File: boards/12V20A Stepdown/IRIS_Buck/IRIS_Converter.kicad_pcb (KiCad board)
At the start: 4 copper layers, 64 x 48 mm, 31 parts, among them J1 TB005-762-02BE, J2 TB005-762-02BE, Q1 CSD17571Q2, Q2 CSD16340Q3, U1 LM25145RGYR

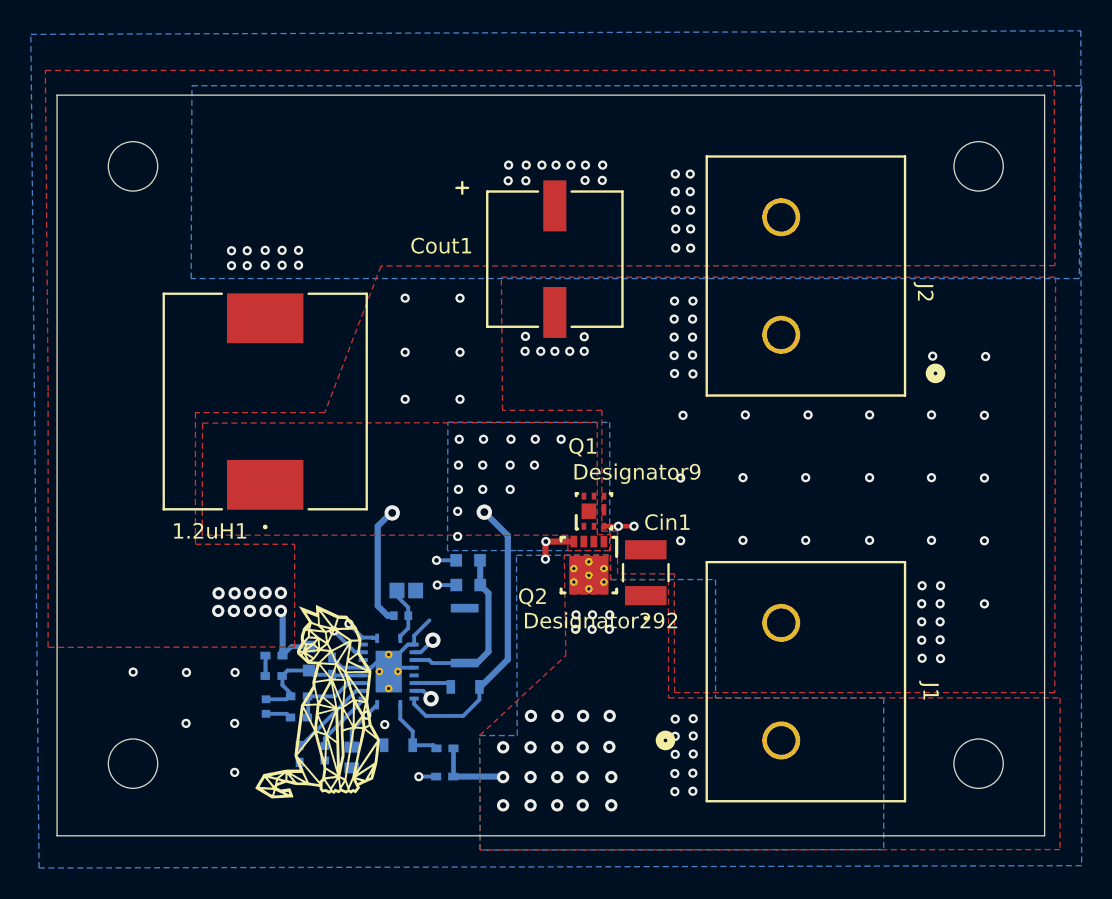
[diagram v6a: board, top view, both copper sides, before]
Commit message: removed backfill on 20a
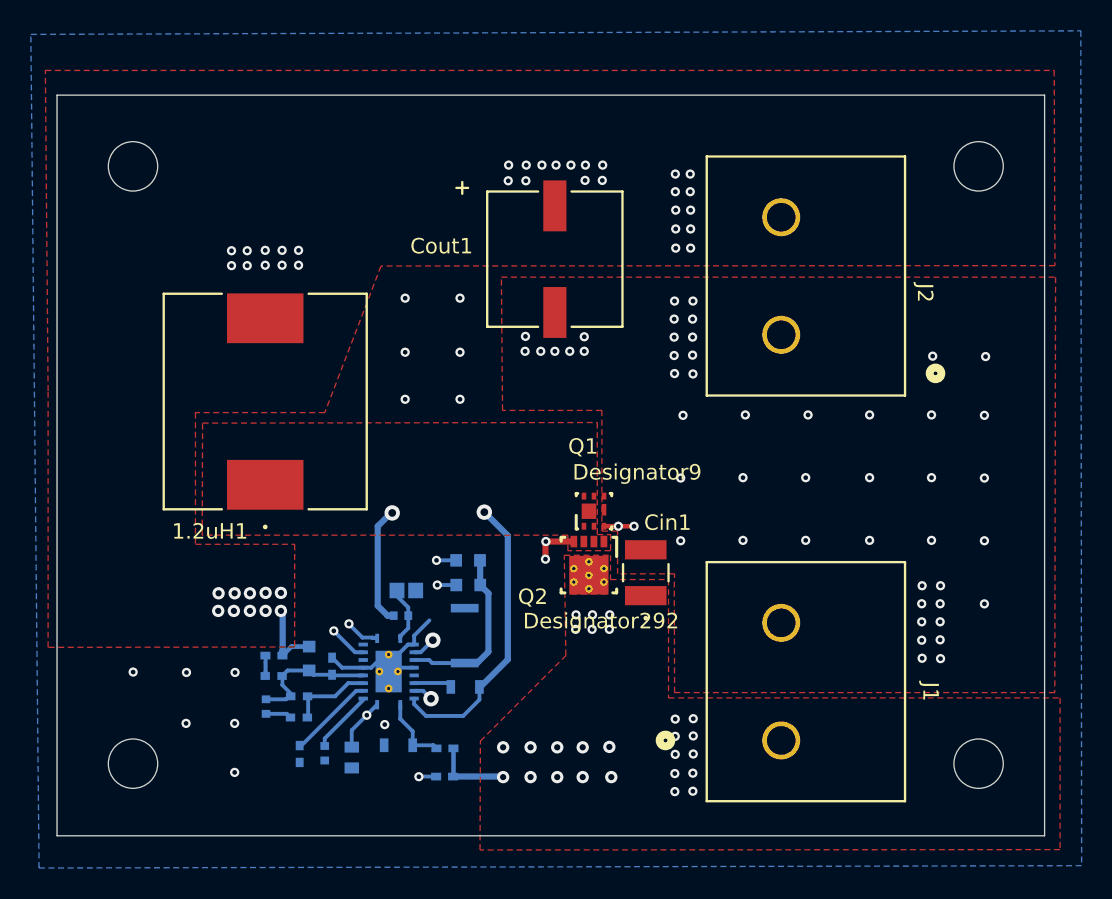
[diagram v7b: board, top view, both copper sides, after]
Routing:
- net /Vin: vias 35 -> 26
- net /SW: vias 16 -> 2
- removed copper zone on B.Cu, net /SW
- removed copper zone on B.Cu, net /Vin
- removed copper zone on B.Cu, net /Vout

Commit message: finished fill zones, silkscreens for 10a and restored component rule areas for 20a
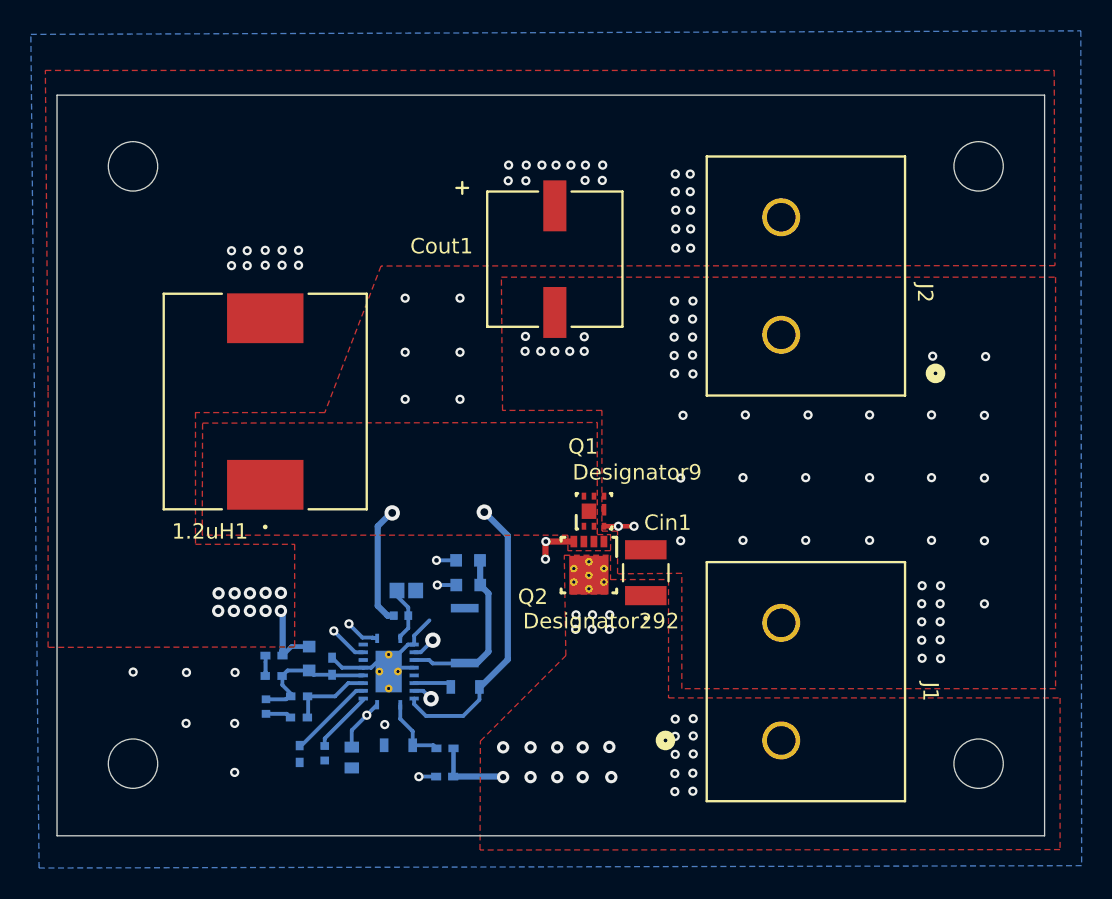
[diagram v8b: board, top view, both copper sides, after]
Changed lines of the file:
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@@
 			(keepout
 				(tracks not_allowed)
-				(vias allowed)
+				(vias not_allowed)
 				(pads allowed)
-				(copperpour allowed)
+				(copperpour not_allowed)
 				(footprints allowed)
 			)
@@
 			(keepout
 				(tracks not_allowed)
-				(vias allowed)
+				(vias not_allowed)
 				(pads allowed)
-				(copperpour allowed)
+				(copperpour not_allowed)
 				(footprints allowed)
 			)
@@
 			(keepout
 				(tracks not_allowed)
-				(vias allowed)
+				(vias not_allowed)
 				(pads allowed)
-				(copperpour allowed)
+				(copperpour not_allowed)
 				(footprints allowed)
 			)
@@
 				(vias not_allowed)
 				(pads allowed)
-				(copperpour allowed)
+				(copperpour not_allowed)
 				(footprints allowed)
 			)
@@
 				(vias not_allowed)
 				(pads allowed)
-				(copperpour allowed)
+				(copperpour not_allowed)
 				(footprints allowed)
 			)
@@
 				(vias not_allowed)
 				(pads allowed)
-				(copperpour allowed)
+				(copperpour not_allowed)
 				(footprints allowed)
 			)
@@
 				(vias not_allowed)
 				(pads allowed)
-				(copperpour allowed)
+				(copperpour not_allowed)
 				(footprints allowed)
 			)
@@
 				(vias not_allowed)
 				(pads allowed)
-				(copperpour allowed)
+				(copperpour not_allowed)
 				(footprints allowed)
 			)
@@
 				(vias not_allowed)
 				(pads allowed)
-				(copperpour allowed)
+				(copperpour not_allowed)
 				(footprints allowed)
 			)
@@
 		(tags "RC0603FR-0720KL ")
 		(property "Reference" "Rpgood1"
-			(at -2.5781 -2.4892 270)
+			(at 2.5654 -2.6416 270)
 			(unlocked yes)
 			(layer "B.SilkS")
@@
 	)
 	(segment
-		(start 93.450802 68.711202)
-		(end 93.6498 68.9102)
-		(width 0.25)
-		(layer "B.Cu")
-		(net 8)
-	)
-	(segment
-		(start 93.6498 68.9102)
-		(end 95.758 68.9102)
+		(start 92.480399 68.711202)
+		(end 93.450802 68.711202)
 		(width 0.25)
 		(layer "B.Cu")
@@
 	)
 	(segment
+		(start 95.7326 68.9356)
+		(end 95.758 68.9102)
+		(width 0.25)
+		(layer "B.Cu")
+		(net 8)
+	)
+	(segment
 		(start 97.2947 64.389)
 		(end 96.7613 63.8556)
@@
 	)
 	(segment
-		(start 92.480399 68.711202)
-		(end 93.450802 68.711202)
+		(start 93.450802 68.711202)
+		(end 93.6752 68.9356)
 		(width 0.25)
 		(layer "B.Cu")
@@
 	)
 	(segment
+		(start 93.6752 68.9356)
+		(end 95.7326 68.9356)
+		(width 0.25)
+		(layer "B.Cu")
+		(net 8)
+	)
+	(segment
 		(start 92.386851 73.336851)
 		(end 91.580401 72.530401)
@@
 		(polygon
 			(pts
-				(xy 98.133156 43.901383) (xy 134.048756 43.901383) (xy 133.997956 70.825383) (xy 109.359956 70.825383)
-				(xy 109.334556 64.018183) (xy 109.359956 63.129183) (xy 105.664 63.129183) (xy 105.664 60.360583)
-				(xy 104.648 60.360583) (xy 104.648 52.537383) (xy 98.209356 52.537383)
+				(xy 98.133156 43.901383) (xy 134.048756 43.901383) (xy 134.048756 70.571383) (xy 109.8296 70.571383)
+				(xy 109.8296 63.0936) (xy 105.664 63.129183) (xy 105.664 60.360583) (xy 104.648 60.360583) (xy 104.648 52.537383)
+				(xy 98.209356 52.537383)
 			)
 		)
